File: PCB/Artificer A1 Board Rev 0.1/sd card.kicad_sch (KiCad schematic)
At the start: 7 parts, among them Q2 2SK3018

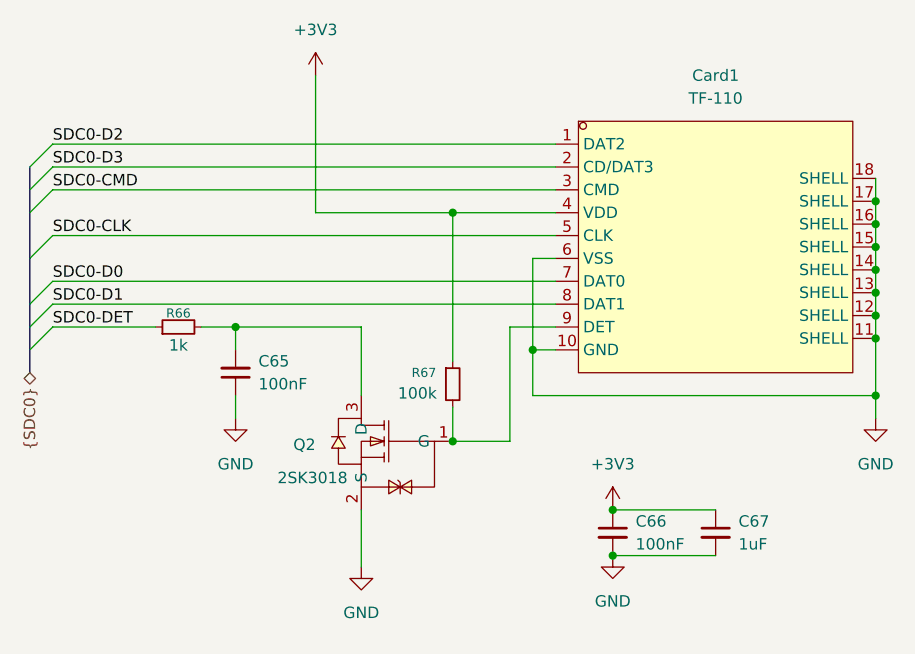
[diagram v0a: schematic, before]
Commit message: cleaned up, kicad 10 & usb c pd
migrated to Kicad 10,
added USB PD for power input
added capacitors inductors and resistor footprints
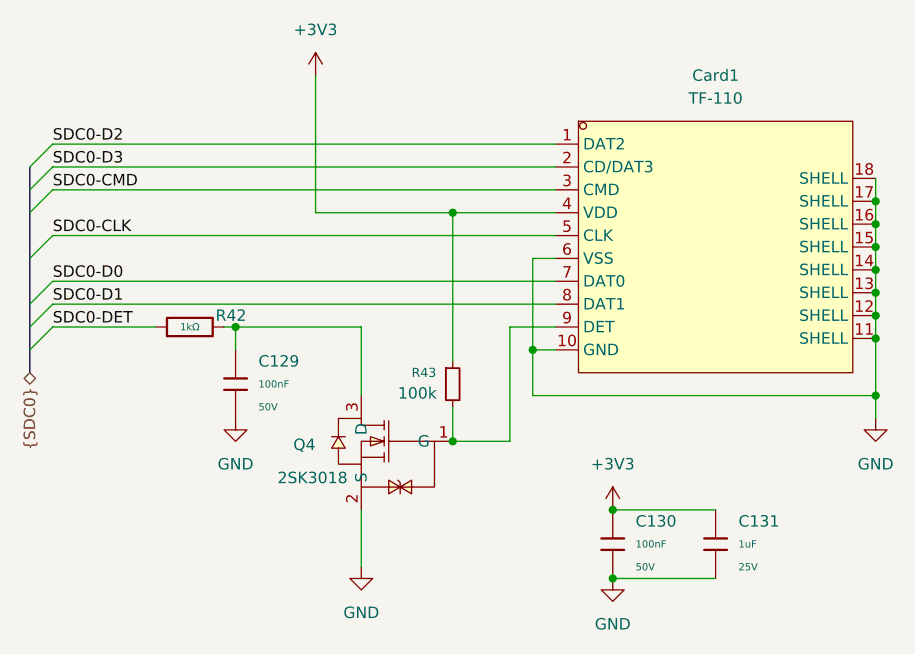
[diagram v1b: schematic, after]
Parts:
- removed C65, C66: 100nF, symbol Device:C_Small
- removed C67: 1uF, symbol Device:C_Small
- removed R66: 1k, symbol Device:R_Small
- added C129, C130: 100nF, PCM_JLCPCB:C_0402, symbol PCM_JLCPCB-Capacitors:0402,100nF,(2)
- added C131: 1uF, PCM_JLCPCB:C_0402, symbol PCM_JLCPCB-Capacitors:0402,1uF
- added R42: 1kΩ, PCM_JLCPCB:R_0402, symbol PCM_JLCPCB-Resistors:0402,1kΩ
- renumbered Q2 to Q4, R67 to R43
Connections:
- net +3V3: now also C130.1, C131.1
- net GND: now also C129.2, C130.2, C131.2
- net SDC0-DET: now also R42.1
- net at Q4.3 (D): now also C129.1, R42.2

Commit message: placed all components
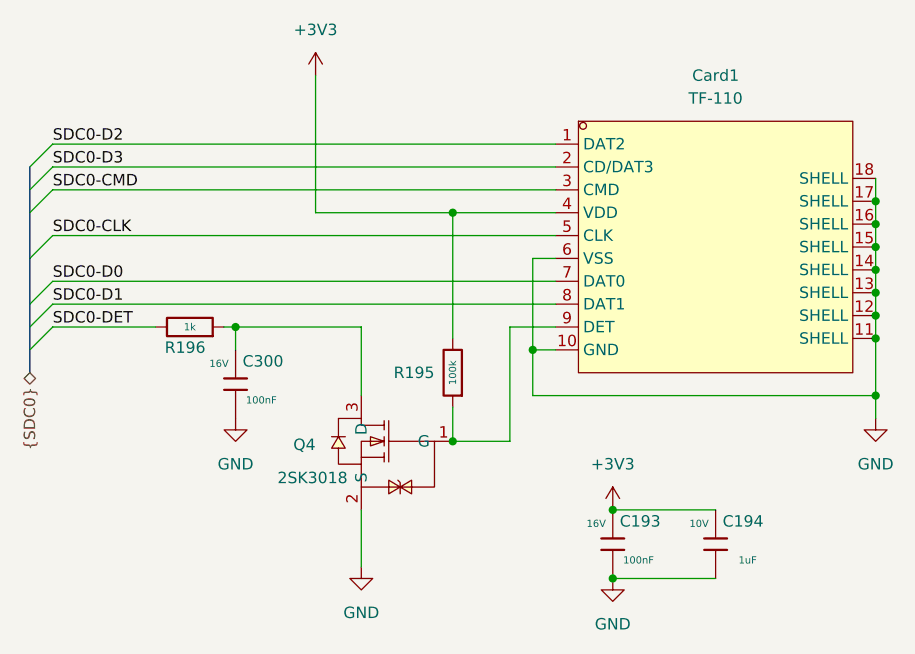
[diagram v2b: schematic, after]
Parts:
- removed C129, C130: 100nF, PCM_JLCPCB:C_0402, symbol PCM_JLCPCB-Capacitors:0402,100nF,(2)
- removed C131: 1uF, PCM_JLCPCB:C_0402, symbol PCM_JLCPCB-Capacitors:0402,1uF
- removed R42: 1kΩ, PCM_JLCPCB:R_0402, symbol PCM_JLCPCB-Resistors:0402,1kΩ
- removed R43: 100k, symbol Device:R_Small
- added C193, C300: 100nF, Capacitor_SMD:C_0201_0603Metric, symbol Cap:JLCPCB_Lib_Blank_Cap
- added C194: 1uF, Capacitor_SMD:C_0201_0603Metric, symbol Cap:JLCPCB_Lib_Blank_Cap
- added R195: 100k, Resistor_SMD:R_0201_0603Metric, symbol Cap:JLCPCB_Res_Custom
- added R196: 1k, Resistor_SMD:R_0201_0603Metric, symbol Cap:JLCPCB_Res_Custom
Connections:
- net +3V3: now also C193.2, C194.2, R195.2
- net GND: now also C193.1, C194.1, C300.1
- net SDC0-DET: now also R196.2
- net at Q4.3 (D): now also C300.2, R196.1
- net at Card1.9 (DET), Q4.1 (G): now also R195.1

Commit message: worked on power pours
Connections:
- net +3V3 renamed VCC-3V3
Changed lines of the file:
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@@
+	)
+	(junction
+		(at 127 128.27)
+		(diameter 0)
+		(color 0 0 0 0)
 	)
 	(junction
@@
 	(junction
 		(at 156.21 96.52)
-		(diameter 0)
-		(color 0 0 0 0)
-	)
-	(junction
-		(at 127 128.27)
 		(diameter 0)
 		(color 0 0 0 0)
@@
 	)
 	(symbol
-		(lib_id "power:+3V3")
-		(at 127 128.27 0)
+		(lib_id "power:+5V")
+		(at 93.98 80.01 0)
 		(unit 1)
 		(body_style 1)
@@
 		(in_pos_files yes)
 		(dnp no)
-		(fields_autoplaced yes)
-		(property "Reference" "#PWR0261"
-			(at 127 132.08 0)
-			(hide yes)
-			(show_name no)
-			(do_not_autoplace no)
-			(effects
-				(font
-					(size 1.27 1.27)
-				)
-			)
-		)
-		(property "Value" "+3V3"
-			(at 127 123.19 0)
+		(property "Reference" "#PWR0259"
+			(at 93.98 83.82 0)
+			(hide yes)
+			(show_name no)
+			(do_not_autoplace no)
+			(effects
+				(font
+					(size 1.27 1.27)
+				)
+			)
+		)
+		(property "Value" "VCC-3V3"
+			(at 93.98 75.946 0)
 			(show_name no)
 			(do_not_autoplace no)
@@
 		)
 		(property "Footprint" ""
-			(at 127 128.27 0)
+			(at 93.98 80.01 0)
 			(hide yes)
 			(show_name no)
@@
 		)
 		(property "Datasheet" ""
-			(at 127 128.27 0)
-			(hide yes)
-			(show_name no)
-			(do_not_autoplace no)
-			(effects
-				(font
-					(size 1.27 1.27)
-				)
-			)
-		)
-		(property "Description" "Power symbol creates a global label with name \"+3V3\""
-			(at 127 128.27 0)
+			(at 93.98 80.01 0)
+			(hide yes)
+			(show_name no)
+			(do_not_autoplace no)
+			(effects
+				(font
+					(size 1.27 1.27)
+				)
+			)
+		)
+		(property "Description" "Power symbol creates a global label with name \"+5V\""
+			(at 93.98 80.01 0)
 			(hide yes)
 			(show_name no)
@@
 			(project "Artificer A1 Board Rev 0.1"
 				(path "/7c37bdb5-94b0-4567-b5ec-a879db855389/9ab7f5fa-ffdb-4acb-910a-53000636bccf"
-					(reference "#PWR0261")
+					(reference "#PWR0259")
 					(unit 1)
 				)
@@
 	)
 	(symbol
-		(lib_id "power:+3V3")
-		(at 93.98 80.01 0)
-		(unit 1)
-		(body_style 1)
-		(exclude_from_sim no)
-		(in_bom yes)
-		(on_board yes)
-		(in_pos_files yes)
-		(dnp no)
-		(fields_autoplaced yes)
-		(property "Reference" "#PWR0259"
-			(at 93.98 83.82 0)
-			(hide yes)
-			(show_name no)
-			(do_not_autoplace no)
-			(effects
-				(font
-					(size 1.27 1.27)
-				)
-			)
-		)
-		(property "Value" "+3V3"
-			(at 93.98 74.93 0)
-			(show_name no)
-			(do_not_autoplace no)
-			(effects
-				(font
-					(size 1.27 1.27)
-				)
-			)
-		)
-		(property "Footprint" ""
-			(at 93.98 80.01 0)
-			(hide yes)
-			(show_name no)
-			(do_not_autoplace no)
-			(effects
-				(font
-					(size 1.27 1.27)
-				)
-			)
-		)
-		(property "Datasheet" ""
-			(at 93.98 80.01 0)
-			(hide yes)
-			(show_name no)
-			(do_not_autoplace no)
-			(effects
-				(font
-					(size 1.27 1.27)
-				)
-			)
-		)
-		(property "Description" "Power symbol creates a global label with name \"+3V3\""
-			(at 93.98 80.01 0)
-			(hide yes)
-			(show_name no)
-			(do_not_autoplace no)
-			(effects
-				(font
-					(size 1.27 1.27)
-				)
-			)
-		)
-		(pin "1"
-		)
-		(instances
-			(project "Artificer A1 Board Rev 0.1"
-				(path "/7c37bdb5-94b0-4567-b5ec-a879db855389/9ab7f5fa-ffdb-4acb-910a-53000636bccf"
-					(reference "#PWR0259")
-					(unit 1)
-				)
-			)
-		)
-	)
-	(symbol
 		(lib_id "Cap:JLCPCB_Res_Custom")
 		(at 109.22 113.03 180)
@@
 					(unit 1)
 				)
+			)
+		)
+	)
+	(symbol
+		(lib_id "power:+5V")
+		(at 127 128.27 0)
+		(unit 1)
+		(body_style 1)
+		(exclude_from_sim no)
+		(in_bom yes)
+		(on_board yes)
+		(in_pos_files yes)
+		(dnp no)
+		(property "Reference" "#PWR0261"
+			(at 127 132.08 0)
+			(hide yes)
+			(show_name no)
+			(do_not_autoplace no)
+			(effects
+				(font
+					(size 1.27 1.27)
+				)
+			)
+		)
+		(property "Value" "VCC-3V3"
+			(at 127 123.698 0)
+			(show_name no)
+			(do_not_autoplace no)
+			(effects
+				(font
+					(size 1.27 1.27)
+				)
+			)
+		)
+		(property "Footprint" ""
+			(at 127 128.27 0)
+			(hide yes)
+			(show_name no)
+			(do_not_autoplace no)
+			(effects
+				(font
+					(size 1.27 1.27)
+				)
+			)
+		)
+		(property "Datasheet" ""
+			(at 127 128.27 0)
+			(hide yes)
+			(show_name no)
+			(do_not_autoplace no)
+			(effects
+				(font
+					(size 1.27 1.27)
+				)
+			)
+		)
+		(property "Description" "Power symbol creates a global label with name \"+5V\""
+			(at 127 128.27 0)
+			(hide yes)
+			(show_name no)
+			(do_not_autoplace no)
+			(effects
+				(font
+					(size 1.27 1.27)
+				)
+			)
+		)
+		(pin "1"
+		)
+		(instances
+			(project "Artificer A1 Board Rev 0.1"
+				(path "/7c37bdb5-94b0-4567-b5ec-a879db855389/9ab7f5fa-ffdb-4acb-910a-53000636bccf"
+					(reference "#PWR0261")
+					(unit 1)
+				)
